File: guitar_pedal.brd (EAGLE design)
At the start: 76.2 x 76.2 mm, 98 parts, among them P1 RM-065, P2 RM-065, P3 RM-065, U1 LM324NSOIC-14, U2 LM324NSOIC-14, U3 LM386N-3, U4 LM386N-3, U5 LM386N-3

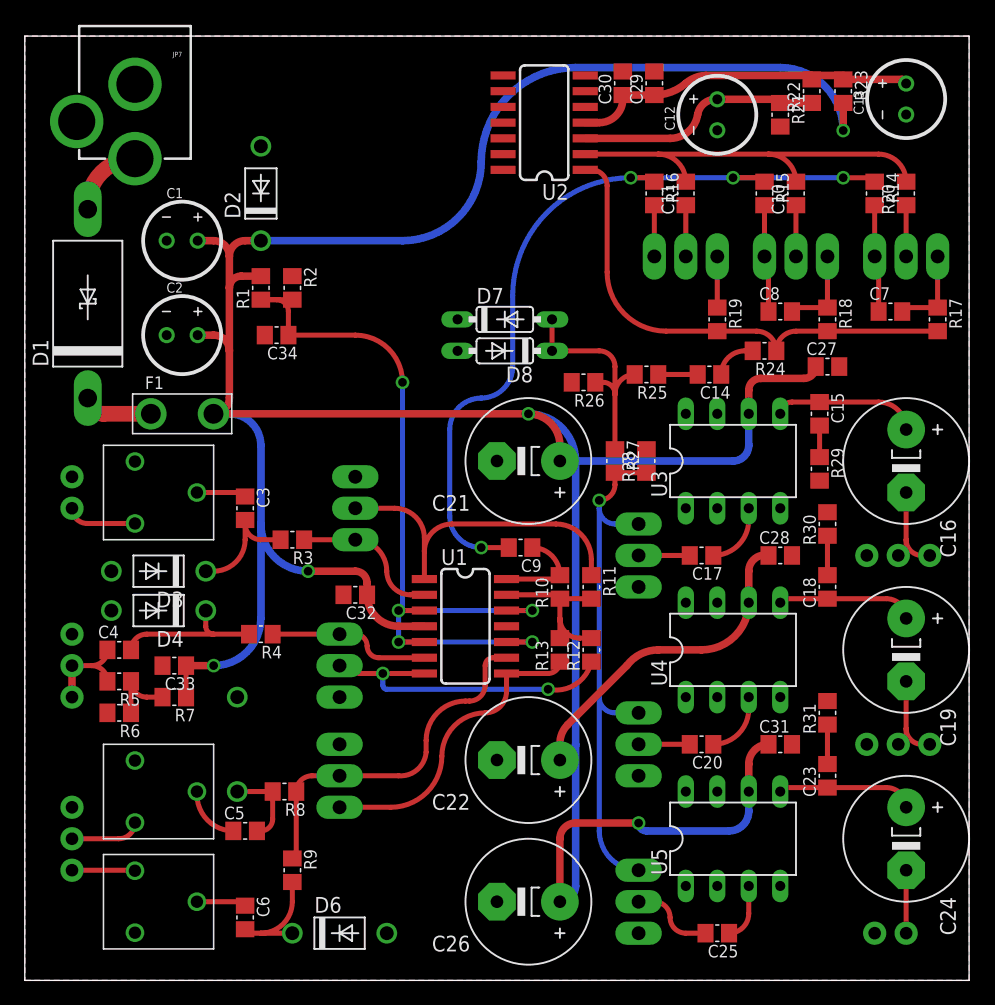
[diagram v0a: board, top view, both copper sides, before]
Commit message: Added most of silk screen. Added vias for debugging. Added ground vias. Added ground plane cutout to through hole components for case with no solder mask.
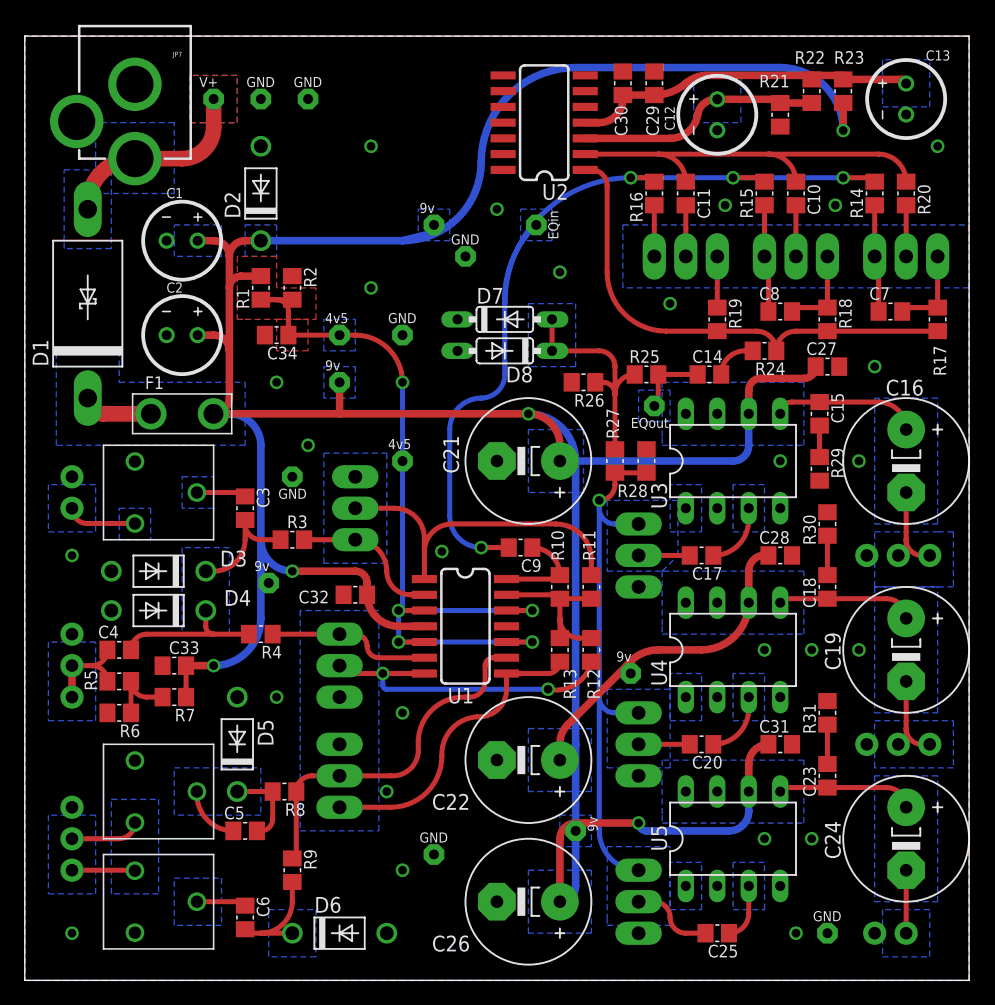
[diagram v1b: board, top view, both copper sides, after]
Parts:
- added V1: V+, Luke:VIA1
- added V10, V11, V12, V13, V14, V15, V16: GND, Luke:VIA1
- added V17: EQout, Luke:VIA1
- added V2: EQin, Luke:VIA1
- added V3, V4, V5, V6, V7: 9v, Luke:VIA1
- added V8, V9: 4v5, Luke:VIA1
- flipped D5 to the top
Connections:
- net +9V: now also V3.P$1, V4.P$1, V5.P$1, V6.P$1, V7.P$1
- net 4.5: now also V8.P$1, V9.P$1
- net GND: now also V10.P$1, V11.P$1, V12.P$1, V13.P$1, V14.P$1, V15.P$1, V16.P$1
- net N$1: now also V1.P$1
- net N$12: now also V2.P$1
- net N$20: now also V17.P$1
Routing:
- net N$1: track 5.66 -> 15.3 mm
- net +9V: track 281.2 -> 288.7 mm
- net N$12: track 63.7 -> 71.0 mm
- net N$20: track 3.18 -> 5.85 mm
- added copper zone on layer 16, net N$39
- added copper zone on layer 16, net N$40
- added copper zone on layer 16, net N$41
- added copper zone on layer 16, net N$42
- added copper zone on layer 1, net N$43
- added copper zone on layer 16, net N$43
- added copper zone on layer 16, net N$44
- added copper zone on layer 16, net N$45
- added copper zone on layer 1, net N$46
- added copper zone on layer 1, net N$47
- added copper zone on layer 16, net N$48
- added copper zone on layer 16, net N$49
- added copper zone on layer 16, net N$50
- added copper zone on layer 16, net N$51
- added copper zone on layer 16, net N$52
- added copper zone on layer 16, net N$53
- added copper zone on layer 16, net N$54
- added copper zone on layer 16, net N$55
- added copper zone on layer 16, net N$56
- added copper zone on layer 16, net N$57
- added copper zone on layer 16, net N$58
- added copper zone on layer 16, net N$59
- added copper zone on layer 16, net N$60
- added copper zone on layer 16, net N$61
- added copper zone on layer 16, net N$62
- added copper zone on layer 16, net N$63
- added copper zone on layer 16, net N$64
- added copper zone on layer 16, net N$65
- added copper zone on layer 16, net N$66
- added copper zone on layer 16, net N$67
- added copper zone on layer 16, net N$68
- added copper zone on layer 16, net N$69
- added copper zone on layer 16, net N$70
- added copper zone on layer 16, net N$71
- added copper zone on layer 16, net N$72
- added copper zone on layer 16, net N$73
- added copper zone on layer 16, net N$74
- added copper zone on layer 16, net N$75
- added copper zone on layer 16, net N$76

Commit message: Finished layout.
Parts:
- added U$1: (no value), Luke:NINJA_TURTLE1
- added U$2: (no value), Luke:NINJA_TURTLE2
- moved V13 14.5 mm to (30.7, 72.1)
- moved V5 11.2 mm to (33.7, 72.1)
- moved C33 3.24 mm to (12.7, 22.2), turned to 270 degrees
- moved R7 2.54 mm to (12.1, 25.4)
- moved V10 2.01 mm to (31.1, 10.8)
- moved V2 1.63 mm to (42.3, 62.2)
- moved C29 1.27 mm to (52.1, 72.4)
- moved C30 1.27 mm to (49.5, 72.4)
- moved R10 1.27 mm to (43.2, 33.0)
- moved R11 1.27 mm to (45.7, 33.0)
- moved R6 0.64 mm to (8.26, 21.6)
- moved C12 0.63 mm to (56.5, 69.8)
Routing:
- net GND: track 0.00 -> 35.5 mm, vias 26 -> 25
- net +9V: track 288.7 -> 295.4 mm
- net OUT_4: track 7.58 -> 5.82 mm
- net N$12: track 71.0 -> 72.3 mm
- net OUT_1: track 26.7 -> 25.5 mm
- net N$7: track 13.4 -> 14.2 mm
- net AMP_3: track 28.1 -> 28.8 mm
- added copper zone on layer 1, net N$100
- added copper zone on layer 1, net N$101
- added copper zone on layer 1, net N$102
- added copper zone on layer 1, net N$103
- added copper zone on layer 1, net N$104
- added copper zone on layer 1, net N$105
- added copper zone on layer 1, net N$106
- added copper zone on layer 1, net N$107
- added copper zone on layer 1, net N$108
- added copper zone on layer 1, net N$109
- added copper zone on layer 1, net N$110
- added copper zone on layer 1, net N$111
- added copper zone on layer 1, net N$112
- added copper zone on layer 1, net N$40
- added copper zone on layer 1, net N$42
- added copper zone on layer 1, net N$51
- added copper zone on layer 1, net N$52
- added copper zone on layer 1, net N$62
- added copper zone on layer 1, net N$63
- added copper zone on layer 1, net N$65
- added copper zone on layer 1, net N$68
- added copper zone on layer 1, net N$70
- added copper zone on layer 1, net N$73
- added copper zone on layer 1, net N$74
- added copper zone on layer 1, net N$75
- added copper zone on layer 1, net N$76
- added copper zone on layer 1, net N$77
- added copper zone on layer 1, net N$78
- added copper zone on layer 1, net N$79
- added copper zone on layer 1, net N$80
- added copper zone on layer 1, net N$81
- added copper zone on layer 1, net N$82
- added copper zone on layer 1, net N$83
- added copper zone on layer 1, net N$84
- added copper zone on layer 1, net N$85
- added copper zone on layer 1, net N$86
- added copper zone on layer 1, net N$87
- added copper zone on layer 1, net N$88
- added copper zone on layer 1, net N$89
- added copper zone on layer 1, net N$90
- added copper zone on layer 1, net N$91
- added copper zone on layer 1, net N$92
- added copper zone on layer 1, net N$93
- added copper zone on layer 1, net N$94
- added copper zone on layer 1, net N$95
- added copper zone on layer 1, net N$96
- added copper zone on layer 1, net N$97
- added copper zone on layer 1, net N$98
- added copper zone on layer 1, net N$99
- removed copper zone on layer 16, net N$40
- removed copper zone on layer 16, net N$51
- removed copper zone on layer 16, net N$52
- removed copper zone on layer 16, net N$62
- removed copper zone on layer 16, net N$63
- removed copper zone on layer 16, net N$65
- removed copper zone on layer 16, net N$68
- removed copper zone on layer 16, net N$70
- removed copper zone on layer 16, net N$73
- removed copper zone on layer 16, net N$74
- removed copper zone on layer 16, net N$75
- removed copper zone on layer 16, net N$76
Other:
- board text added: "AC & LG"
- board text added: "AUX"
- board text added: "AUX GAIN"
- board text added: "AUX IN"
- board text added: "AUX VOL"
- board text added: "BASS"
- board text added: "GTR"
- board text added: "GTR GAIN"
- board text added: "GTR IN"
- board text added: "GTR VOL"
- board text added: "MID"
- board text added: "TREB"
- board text added: "Two Turtle Gang"
- board text added: "XLR"
- board text added: "XLR GAIN"
- board text added: "XLR IN"
- board text added: "XLR VOL"
